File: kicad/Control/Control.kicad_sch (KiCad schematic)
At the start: 18 parts, among them J1 Backplane Signal, J2 Backplane Bus, U1 27C64, U10 74LS377, U11 74LS253, U2 27C64, U3 27C64, U4 27C64, U5 27C64, U6 74LS273, U7 74LS377, U8 74LS377, U9 74LS377

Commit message: Start migrating over to DIN41612 connectors
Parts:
- added U12, U13, U14, U15, U16, U17: 74LS253, symbol 74xx:74LS253
- added U18: 74LS257, symbol 74xx:74LS257
- added U19, U20, U21: 74LS377, symbol 74xx:74LS377
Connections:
- net *LATCH_AC: now also U7.9 (Q3)
- net *LATCH_IR: now also U7.2 (Q0), U19.1 (~{E}), U20.1 (~{E}), U21.1 (~{E})
- net *LATCH_MA: now also U7.5 (Q1)
- net *LATCH_MB: now also U7.16 (Q6)
- net *LATCH_MQ: now also U7.15 (Q5)
- net *LATCH_PC: now also U7.6 (Q2)
- net *LATCH_STEP: now also U7.12 (Q4)
- net +5V: now also U12.16 (VCC), U13.16 (VCC), U14.16 (VCC), U15.16 (VCC), U16.16 (VCC), U17.16 (VCC), U18.16 (VCC), U19.20 (VCC), U20.20 (VCC), U21.20 (VCC)
- net ADDR_MODE0: now also U8.15 (Q5)
- net ADDR_MODE1: now also U8.16 (Q6)
- net CLK: now also U19.11 (CP), U20.11 (CP), U21.11 (CP)
- net CTL_CONST: now also U8.19 (Q7)
- net D0: now also U19.3 (D0)
- net D1: now also U19.4 (D1)
- net D10: now also U20.7 (D2)
- net D11: now also U20.8 (D3)
- net D12: now also U20.13 (D4)
- net D13: now also U20.14 (D5)
- net D14: now also U20.17 (D6)
- net D15: now also U20.18 (D7)
- net D2: now also U19.7 (D2)
- net D3: now also U19.8 (D3)
- net D4: now also U19.13 (D4)
- net D5: now also U19.14 (D5)
- net D6: now also U19.17 (D6)
- net D7: now also U19.18 (D7)
- net D8: now also U20.3 (D0)
- net D9: now also U20.4 (D1)
- net DRQ_GRANT: now also U9.9 (Q3)
- net GND: now also U11.1 (OEa), U11.15 (OEb), U12.1 (OEa), U12.15 (OEb), U12.8 (GND), U13.1 (OEa), U13.15 (OEb), U13.8 (GND), U14.1 (OEa), U14.15 (OEb), U14.8 (GND), U15.1 (OEa), U15.15 (OEb), U15.8 (GND), U16.1 (OEa), U16.15 (OEb), U16.8 (GND), U17.1 (OEa), U17.15 (OEb), U17.8 (GND), U18.15 (OE), U18.8 (GND), U19.10 (GND), U20.10 (GND), U21.10 (GND)
- net HALT: now also U8.12 (Q4)
- net INT_DETECT: now also U9.16 (Q6)
- net IOT_PULSE: now also U9.6 (Q2)
- net JMP_I_DETECT: now also U9.15 (Q5)
- net READ_IN_PULSE: now also U9.19 (Q7)
- net REQ_ADDR: now also U9.12 (Q4)
- net SELECT_PCMA: now also U8.9 (Q3)
- net ST0: now also U6.2 (Q0)
- net ST1: now also U11.7 (Za)
- net ST10: now also U15.9 (Zb)
- net ST11: now also U11.14 (A0), U6.16 (Q6), U12.14 (A0), U13.14 (A0), U14.14 (A0), U15.14 (A0)
- net ST12: now also U11.2 (A1), U6.19 (Q7), U12.2 (A1), U13.2 (A1), U14.2 (A1), U15.2 (A1)
- net ST2: now also U11.9 (Zb)
- net ST3: now also U12.7 (Za)
- net ST4: now also U12.9 (Zb)
- net ST5: now also U13.7 (Za)
- net ST6: now also U13.9 (Zb)
- net ST7: now also U14.7 (Za)
- net ST8: now also U14.9 (Zb)
- net ST9: now also U15.7 (Za)
- net WRITE_CORE: now also U7.19 (Q7)
- net at U11.10 (I0b): now also U11.11 (I1b), U11.13 (I3b), U6.6 (Q2)
- net at U11.3 (I3a): now also U11.5 (I1a), U11.6 (I0a), U6.5 (Q1)
- net at U6.12 (Q4): now also U12.10 (I0b), U12.13 (I3b), U16.14 (A0), U17.14 (A0)
- net at U6.15 (Q5): now also U13.3 (I3a), U13.6 (I0a), U16.2 (A1), U17.2 (A1), U18.1 (S)
- net at U6.9 (Q3): now also U12.3 (I3a), U12.6 (I0a)
- new net: U15.6 (I0a), U17.7 (Za)
- new net: U15.10 (I0b), U17.9 (Zb)
- new net: U14.10 (I0b), U16.9 (Zb)
- new net: U14.13 (I3b), U18.7 (Zb)
- new net: U14.3 (I3a), U18.4 (Za)
- new net: U14.6 (I0a), U16.7 (Za)
- new net: U15.3 (I3a), U18.12 (Zc)
- new net: U15.13 (I3b), U18.9 (Zd)
- no-connect marks 72 -> 53
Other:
- moved on the sheet: J1, J2, U11

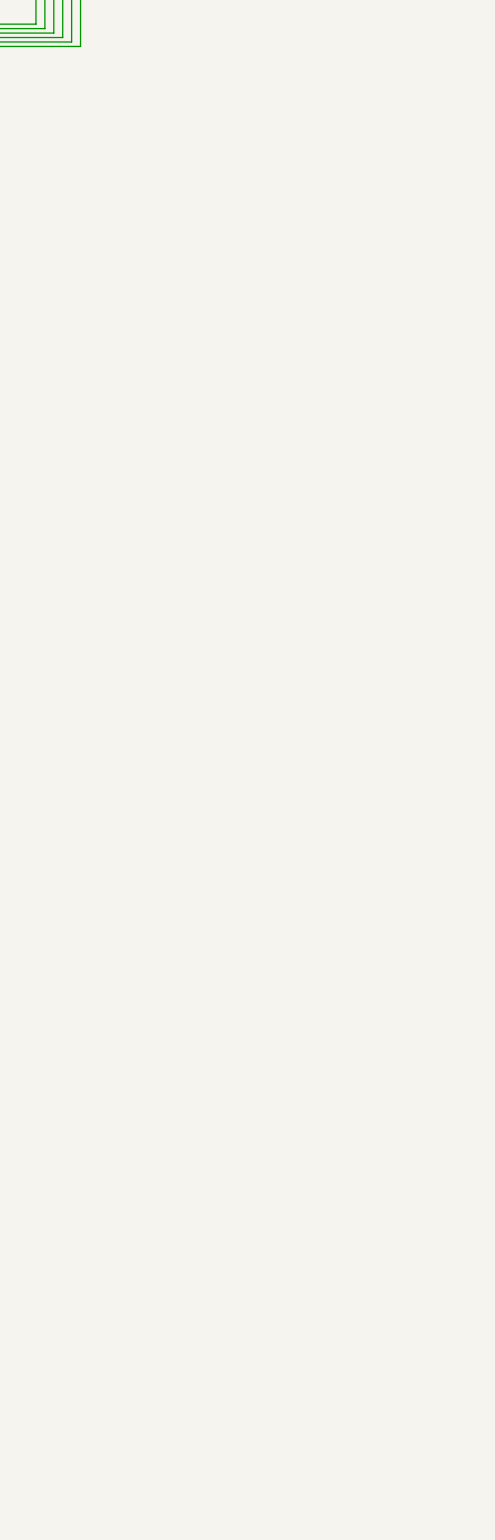
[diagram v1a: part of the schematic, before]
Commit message: Continue connector migration
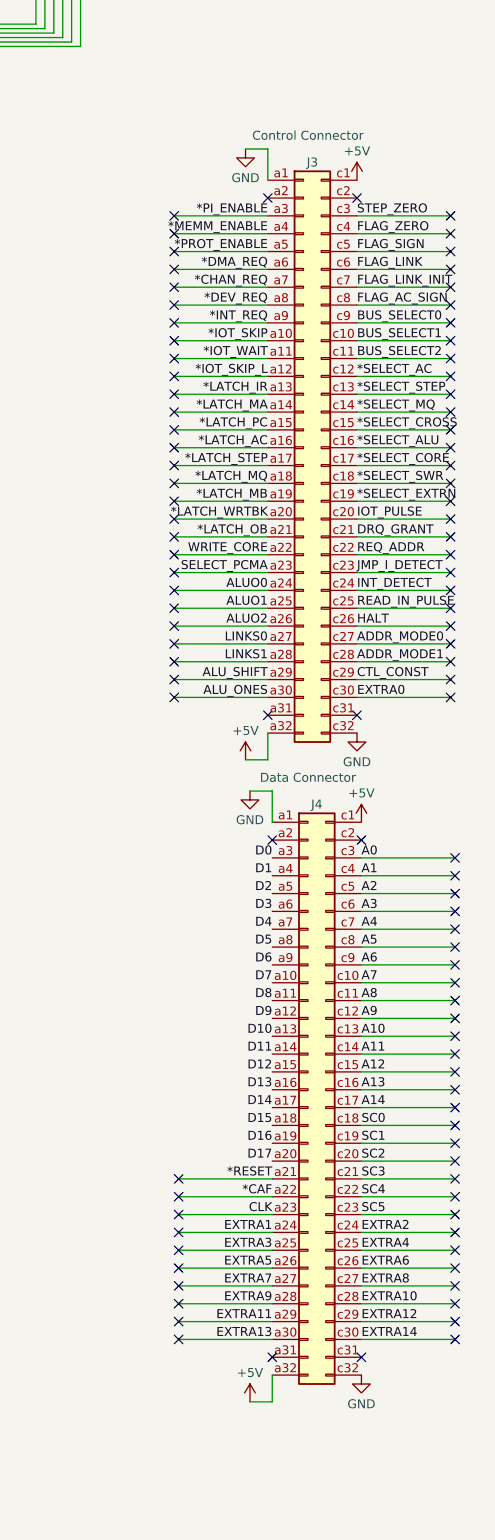
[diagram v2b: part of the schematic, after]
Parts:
- added J3: Control Connector, symbol Connector:DIN41612_02x32_AC
- added J4: Data Connector, symbol Connector:DIN41612_02x32_AC
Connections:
- net *CHAN_REQ: now also J3.a7 (Pin_a7)
- net *DEV_REQ: now also J3.a8 (Pin_a8)
- net *DMA_REQ: now also J3.a6 (Pin_a6)
- net *INT_REQ: now also J3.a9 (Pin_a9)
- net *IOT_SKIP: now also J3.a10 (Pin_a10)
- net *IOT_SKIP_L: now also J3.a12 (Pin_a12)
- net *IOT_WAIT: now also J3.a11 (Pin_a11)
- net *LATCH_AC: now also J3.a16 (Pin_a16)
- net *LATCH_IR: now also J3.a13 (Pin_a13)
- net *LATCH_MA: now also J3.a14 (Pin_a14)
- net *LATCH_MB: now also J3.a19 (Pin_a19)
- net *LATCH_MQ: now also J3.a18 (Pin_a18)
- net *LATCH_OB: now also J3.a21 (Pin_a21)
- net *LATCH_PC: now also J3.a15 (Pin_a15)
- net *LATCH_STEP: now also J3.a17 (Pin_a17)
- net *LATCH_WRTBK: now also J3.a20 (Pin_a20)
- net *MEMM_ENABLE: now also J3.a4 (Pin_a4)
- net *PI_ENABLE: now also J3.a3 (Pin_a3)
- net *PROT_ENABLE: now also J3.a5 (Pin_a5)
- net *RESET: now also J4.a21 (Pin_a21)
- net *SELECT_ALU: now also J3.c16 (Pin_c16)
- net *SELECT_CORE: now also J3.c17 (Pin_c17)
- net *SELECT_EXTRN: now also J3.c19 (Pin_c19)
- net *SELECT_SWR: now also J3.c18 (Pin_c18)
- net +5V: now also J3.a32 (Pin_a32), J3.c1 (Pin_c1), J4.a32 (Pin_a32), J4.c1 (Pin_c1)
- net A0: now also J4.c3 (Pin_c3)
- net A1: now also J4.c4 (Pin_c4)
- net A10: now also J4.c13 (Pin_c13)
- net A11: now also J4.c14 (Pin_c14)
- net A12: now also J4.c15 (Pin_c15)
- net A13: now also J4.c16 (Pin_c16)
- net A14: now also J4.c17 (Pin_c17)
- net A2: now also J4.c5 (Pin_c5)
- net A3: now also J4.c6 (Pin_c6)
- net A4: now also J4.c7 (Pin_c7)
- net A5: now also J4.c8 (Pin_c8)
- net A6: now also J4.c9 (Pin_c9)
- net A7: now also J4.c10 (Pin_c10)
- net A8: now also J4.c11 (Pin_c11)
- net A9: now also J4.c12 (Pin_c12)
- net ADDR_MODE0: now also J3.c27 (Pin_c27)
- net ADDR_MODE1: now also J3.c28 (Pin_c28)
- net ALUO0: now also J3.a24 (Pin_a24)
- net ALUO1: now also J3.a25 (Pin_a25)
- net ALUO2: now also J3.a26 (Pin_a26)
- net ALU_ONES: now also J3.a30 (Pin_a30)
- net ALU_SHIFT: now also J3.a29 (Pin_a29)
- net BUS_SELECT0: now also J3.c9 (Pin_c9)
- net BUS_SELECT1: now also J3.c10 (Pin_c10)
- net BUS_SELECT2: now also J3.c11 (Pin_c11)
- net CLK: now also J4.a23 (Pin_a23)
- net CTL_CONST: now also J3.c29 (Pin_c29)
- net D0: now also J4.a3 (Pin_a3)
- net D1: now also J4.a4 (Pin_a4)
- net D10: now also J4.a13 (Pin_a13)
- net D11: now also J4.a14 (Pin_a14)
- net D12: now also J4.a15 (Pin_a15)
- net D13: now also J4.a16 (Pin_a16)
- net D14: now also J4.a17 (Pin_a17)
- net D15: now also J4.a18 (Pin_a18)
- net D16: now also J4.a19 (Pin_a19)
- net D17: now also J4.a20 (Pin_a20)
- net D2: now also J4.a5 (Pin_a5)
- net D3: now also J4.a6 (Pin_a6)
- net D4: now also J4.a7 (Pin_a7)
- net D5: now also J4.a8 (Pin_a8)
- net D6: now also J4.a9 (Pin_a9)
- net D7: now also J4.a10 (Pin_a10)
- net D8: now also J4.a11 (Pin_a11)
- net D9: now also J4.a12 (Pin_a12)
- net DRQ_GRANT: now also J3.c21 (Pin_c21)
- net FLAG_AC_SIGN: now also J3.c8 (Pin_c8)
- net FLAG_LINK: now also J3.c6 (Pin_c6)
- net FLAG_LINK_INIT: now also J3.c7 (Pin_c7)
- net FLAG_SIGN: now also J3.c5 (Pin_c5)
- net FLAG_ZERO: now also J3.c4 (Pin_c4)
- net GND: now also J3.a1 (Pin_a1), J3.c32 (Pin_c32), J4.a1 (Pin_a1), J4.c32 (Pin_c32)
- net HALT: now also J3.c26 (Pin_c26)
- net INT_DETECT: now also J3.c24 (Pin_c24)
- net IOT_PULSE: now also J3.c20 (Pin_c20)
- net JMP_I_DETECT: now also J3.c23 (Pin_c23)
- net LINKS0: now also J3.a27 (Pin_a27)
- net LINKS1: now also J3.a28 (Pin_a28)
- net READ_IN_PULSE: now also J3.c25 (Pin_c25)
- net REQ_ADDR: now also J3.c22 (Pin_c22)
- net SELECT_PCMA: now also J3.a23 (Pin_a23)
- net STEP_ZERO: now also J3.c3 (Pin_c3)
- net WRITE_CORE: now also J3.a22 (Pin_a22)
- new net *CAF: J4.a22 (Pin_a22)
- new net *SELECT_AC: J3.c12 (Pin_c12)
- new net *SELECT_CROSS: J3.c15 (Pin_c15)
- new net *SELECT_MQ: J3.c14 (Pin_c14)
- new net *SELECT_STEP: J3.c13 (Pin_c13)
- new net EXTRA0: J3.c30 (Pin_c30)
- new net EXTRA1: J4.a24 (Pin_a24)
- new net EXTRA10: J4.c28 (Pin_c28)
- new net EXTRA11: J4.a29 (Pin_a29)
- new net EXTRA12: J4.c29 (Pin_c29)
- new net EXTRA13: J4.a30 (Pin_a30)
- new net EXTRA14: J4.c30 (Pin_c30)
- new net EXTRA2: J4.c24 (Pin_c24)
- new net EXTRA3: J4.a25 (Pin_a25)
- new net EXTRA4: J4.c25 (Pin_c25)
- new net EXTRA5: J4.a26 (Pin_a26)
- new net EXTRA6: J4.c26 (Pin_c26)
- new net EXTRA7: J4.a27 (Pin_a27)
- new net EXTRA8: J4.c27 (Pin_c27)
- new net EXTRA9: J4.a28 (Pin_a28)
- new net SC0: J4.c18 (Pin_c18)
- new net SC1: J4.c19 (Pin_c19)
- new net SC2: J4.c20 (Pin_c20)
- new net SC3: J4.c21 (Pin_c21)
- new net SC4: J4.c22 (Pin_c22)
- new net SC5: J4.c23 (Pin_c23)
- no-connect marks 53 -> 155

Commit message: Rework CAF and continue control board schematic
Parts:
- removed J1: Backplane Signal, symbol Connector_Generic:Conn_02x30_Odd_Even
- removed J2: Backplane Bus, symbol Connector_Generic:Conn_02x20_Odd_Even
- added R6: 4.7K, symbol Device:R
- added U22: 74LS138, symbol 74xx:74LS138
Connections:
- net EXTRA10 is gone; now on net MA_AUTO_INX: J4.c28 (Pin_c28)
- net EXTRA11 is gone; now on net FP0: J4.a29 (Pin_a29)
- net EXTRA12 is gone; now on net FP1: J4.c29 (Pin_c29)
- net EXTRA13 is gone; now on net FP2: J4.a30 (Pin_a30)
- net EXTRA14 is gone; now on net FP3: J4.c30 (Pin_c30)
- net EXTRA9 is gone; now on net REST_PEND: J4.a28 (Pin_a28)
- net *CHAN_REQ: now also U16.11 (I1b)
- net *DEV_REQ: now also U17.4 (I2a)
- net *DMA_REQ: now also U16.5 (I1a)
- net *INT_REQ: now also U17.12 (I2b)
- net *IOT_SKIP_L: now also U17.5 (I1a)
- net *IOT_WAIT: now also U17.11 (I1b)
- net *LATCH_OB: now also U10.19 (Q7)
- net *LATCH_WRTBK: now also U9.2 (Q0)
- net *SELECT_AC: now also U22.15 (O0)
- net *SELECT_ALU: now also U22.11 (O4)
- net *SELECT_CORE: now also U22.10 (O5)
- net *SELECT_CROSS: now also U22.12 (O3)
- net *SELECT_EXTRN: now also U22.7 (O7)
- net *SELECT_MQ: now also U22.13 (O2)
- net *SELECT_STEP: now also U22.14 (O1)
- net *SELECT_SWR: now also U22.9 (O6)
- net +5V: now also R6.2, U22.16 (VCC)
- net ALUO0: now also U10.2 (Q0)
- net ALUO1: now also U10.5 (Q1)
- net ALUO2: now also U10.6 (Q2)
- net ALU_ONES: now also U10.16 (Q6)
- net ALU_SHIFT: now also U10.15 (Q5)
- net BUS_SELECT0: now also U8.2 (Q0), U22.1 (A0)
- net BUS_SELECT1: now also U8.5 (Q1), U22.2 (A1)
- net BUS_SELECT2: now also U8.6 (Q2), U22.3 (A2)
- net D16: now also U21.3 (D0)
- net D17: now also U21.4 (D1)
- net EXTRA0: now also U9.5 (Q1)
- net FLAG_AC_SIGN: now also U18.10 (I1d)
- net FLAG_LINK: now also U13.13 (I3b), U15.12 (I2b)
- net FLAG_LINK_INIT: now also U18.11 (I0d)
- net FLAG_ZERO: now also U16.4 (I2a)
- net GND: now also U21.13 (D4), U21.14 (D5), U21.17 (D6), U21.18 (D7), U21.7 (D2), U21.8 (D3), U22.4 (E1), U22.5 (E2), U22.8 (GND)
- net LINKS0: now also U10.9 (Q3)
- net LINKS1: now also U10.12 (Q4)
- net STEP_ZERO: now also U13.10 (I0b)
- net at U13.11 (I1b): now also U20.19 (Q7)
- net at U13.12 (I2b): now also U19.15 (Q5)
- net at U13.4 (I2a): now also U19.12 (Q4)
- net at U13.5 (I1a): now also U20.16 (Q6)
- net at U11.12 (I2b): now also U16.13 (I3b), U19.5 (Q1)
- net at U11.4 (I2a): now also U16.3 (I3a), U19.2 (Q0)
- net at U19.16 (Q6): now also U18.2 (I0a)
- net at U19.19 (Q7): now also U18.5 (I0b)
- net at U19.6 (Q2): now also U12.4 (I2a), U17.3 (I3a)
- net at U19.9 (Q3): now also U12.12 (I2b), U12.5 (I1a)
- net at U20.12 (Q4): now also U15.4 (I2a), U17.13 (I3b)
- net at U20.15 (Q5): now also U12.11 (I1b)
- net at U20.2 (Q0): now also U18.14 (I0c)
- net at U20.5 (Q1): now also U18.3 (I1a)
- net at U20.6 (Q2): now also U14.4 (I2a), U18.6 (I1b)
- net at U20.9 (Q3): now also U14.12 (I2b), U18.13 (I1c)
- net FP3: now reaches U17.10 (I0b)
- net FP2: now reaches U17.6 (I0a)
- net at U14.11 (I1b): now also U21.5 (Q1)
- net at U14.5 (I1a): now also U21.2 (Q0)
- net FP1: now reaches U16.10 (I0b)
- net FP0: now reaches U16.6 (I0a)
- net MA_AUTO_INX: now reaches U15.11 (I1b)
- net REST_PEND: now reaches U15.5 (I1a)
- new net: R6.1, U22.6 (E3)
- no-connect marks 155 -> 49
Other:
- moved on the sheet: J3, J4, U11, U12, U13, U14, U15, U16, U17, U18, U19, U20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

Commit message: Finish control logic
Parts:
- added C1, C10, C11, C12, C13, C14, C15, C16, C17, C18, C19, C2, C20, C21, C22, C23, C24, C25, C26, C3, C4, C5, C6, C7, C8, C9: 0.1uF, symbol Device:C
- added C20: 100 uF, Capacitor_THT:CP_Radial_D6.3mm_P2.50mm, symbol Device:C_Polarized
- added R10, R7, R8, R9: 4.7K, symbol Device:R
- added U23: 74LS32, symbol 74xx:74LS32
- added U24: 74LS08, symbol 74xx:74LS08
- added U25: 74LS86, symbol 74xx:74LS86
- added U26: 74LS74, symbol 74xx:74LS74
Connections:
- net *IOT_WAIT: now also U26.2 (D); no longer U17.11 (I1b)
- net +5V: now also C1.1, C10.1, C11.1, C12.1, C13.1, C14.1, C15.1, C16.1, C17.1, C18.1, C19.1, C2.1, C20.1, C20.1, C21.1, C22.1, C23.1, C24.1, C25.1, C26.1, C3.1, C4.1, C5.1, C6.1, C7.1, C8.1, C9.1, R10.2, R7.2, R8.2, R9.2, U23.14 (VCC), U24.14 (VCC), U25.14 (VCC), U26.14 (VCC)
- net CLK: now also U9.11 (CP), U26.11 (C), U26.3 (C)
- net FLAG_LINK: now also U24.9
- net FLAG_SIGN: now also U24.1
- net FLAG_ZERO: now also U24.4
- net GND: now also C1.2, C10.2, C11.2, C12.2, C13.2, C14.2, C15.2, C16.2, C17.2, C18.2, C19.2, C2.2, C20.2, C20.2, C21.2, C22.2, C23.2, C24.2, C25.2, C26.2, C3.2, C4.2, C5.2, C6.2, C7.2, C8.2, C9.2, U23.10, U23.12, U23.13, U23.7 (GND), U23.9, U24.12, U24.13, U24.7 (GND), U25.10, U25.12, U25.13, U25.4, U25.5, U25.7 (GND), U25.9, U26.12 (D), U26.7 (GND)
- net IR15: now reaches U13.11 (I1b), U20.19 (Q7)
- net IR5: now reaches U13.12 (I2b), U19.15 (Q5)
- net STEP5: now reaches U13.3 (I3a), U13.6 (I0a), U16.2 (A1), U17.2 (A1), U18.1 (S), U6.15 (Q5)
- net IR4: now reaches U13.4 (I2a), U19.12 (Q4)
- net IR14: now reaches U13.5 (I1a), U20.16 (Q6)
- net STEP2: now reaches U11.10 (I0b), U11.11 (I1b), U11.13 (I3b), U6.6 (Q2)
- net IR1: now reaches U11.12 (I2b), U16.13 (I3b), U19.5 (Q1)
- net STEP1: now reaches U11.3 (I3a), U11.5 (I1a), U11.6 (I0a), U6.5 (Q1)
- net IR0: now reaches U11.4 (I2a), U16.3 (I3a), U19.2 (Q0)
- net IR6: now reaches U18.2 (I0a), U19.16 (Q6)
- net IR6: now also U24.2
- net IR7: now reaches U18.5 (I0b), U19.19 (Q7)
- net IR7: now also U24.5
- net IR2: now reaches U12.4 (I2a), U17.3 (I3a), U19.6 (Q2)
- net IR3: now reaches U12.12 (I2b), U12.5 (I1a), U19.9 (Q3)
- net IR12: now reaches U15.4 (I2a), U17.13 (I3b), U20.12 (Q4)
- net IR13: now reaches U12.11 (I1b), U20.15 (Q5)
- net IR8: now reaches U18.14 (I0c), U20.2 (Q0)
- net IR8: now also U24.10
- net IR9: now reaches U18.3 (I1a), U20.5 (Q1)
- net IR9: now also U25.2
- net IR10: now reaches U14.4 (I2a), U18.6 (I1b), U20.6 (Q2)
- net IR11: now reaches U14.12 (I2b), U18.13 (I1c), U20.9 (Q3)
- net STEP4: now reaches U12.10 (I0b), U12.13 (I3b), U16.14 (A0), U17.14 (A0), U6.12 (Q4)
- net STEP3: now reaches U12.3 (I3a), U12.6 (I0a), U6.9 (Q3)
- net IR17: now reaches U14.11 (I1b), U21.5 (Q1)
- net IR16: now reaches U14.5 (I1a), U21.2 (Q0)
- net OPR_SKIP: now reaches U16.12 (I2b)
- net OPR_SKIP: now also U25.3
- new net: R9.1, U26.10 (~{S})
- new net: R10.1, U26.13 (~{R})
- new net: R8.1, U26.1 (~{R})
- new net: U23.2, U24.3
- new net: U23.1, U24.6
- new net: U23.3, U23.5
- new net: U23.4, U24.8
- new net: U23.6, U25.1
- new net: U17.11 (I1b), U26.6 (~{Q})
- new net: R7.1, U26.4 (~{S})
- no-connect marks 49 -> 57
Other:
- note added: "IR"
- note added: "Register"
